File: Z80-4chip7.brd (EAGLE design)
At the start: 99.7 x 99.7 mm, 99 parts, among them IC1 Z84C00xx (-Z80-), IC2 CXK581000 (128k * 8), IC4 7400N, M1 WIRE-VIA8, U1 ATMEGA32A-PU

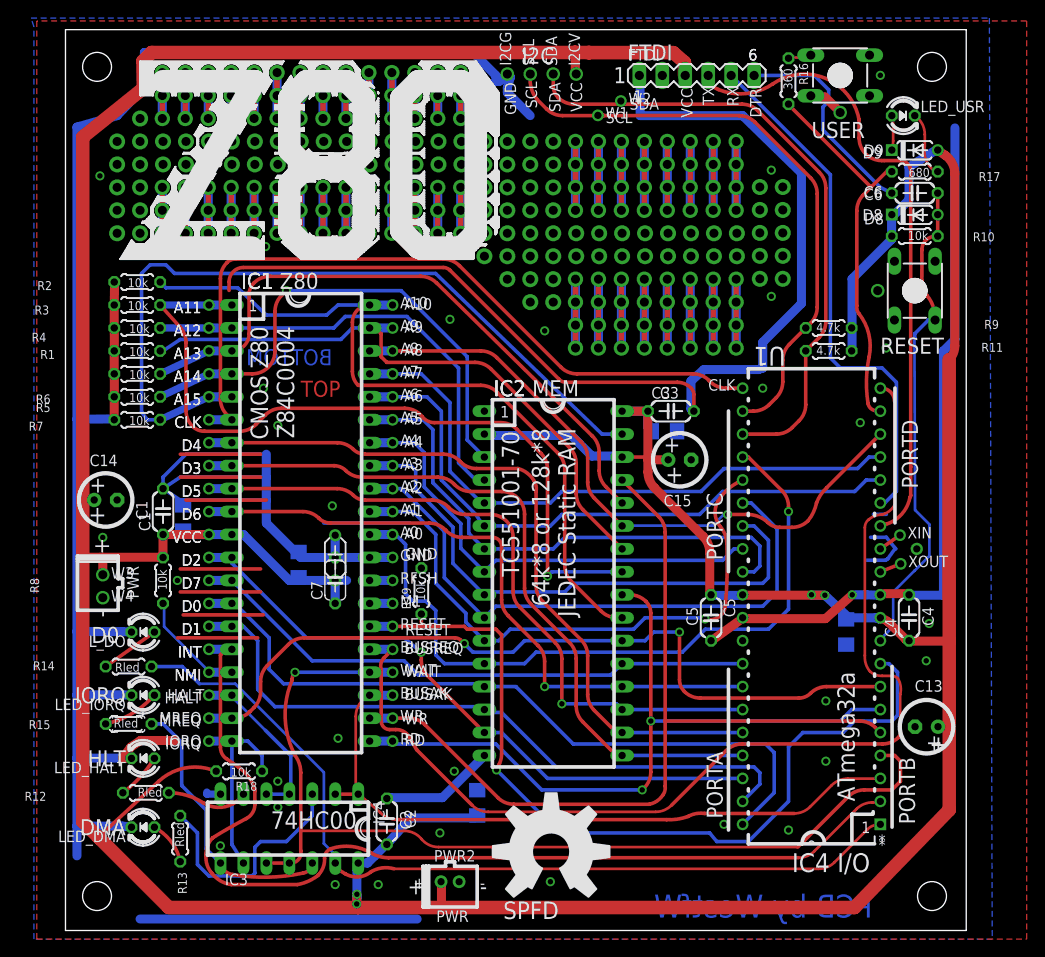
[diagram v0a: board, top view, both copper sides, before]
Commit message: Mod silkscreen: RTS->DTR, add "Version 2."  Generate Gerbers-V2.
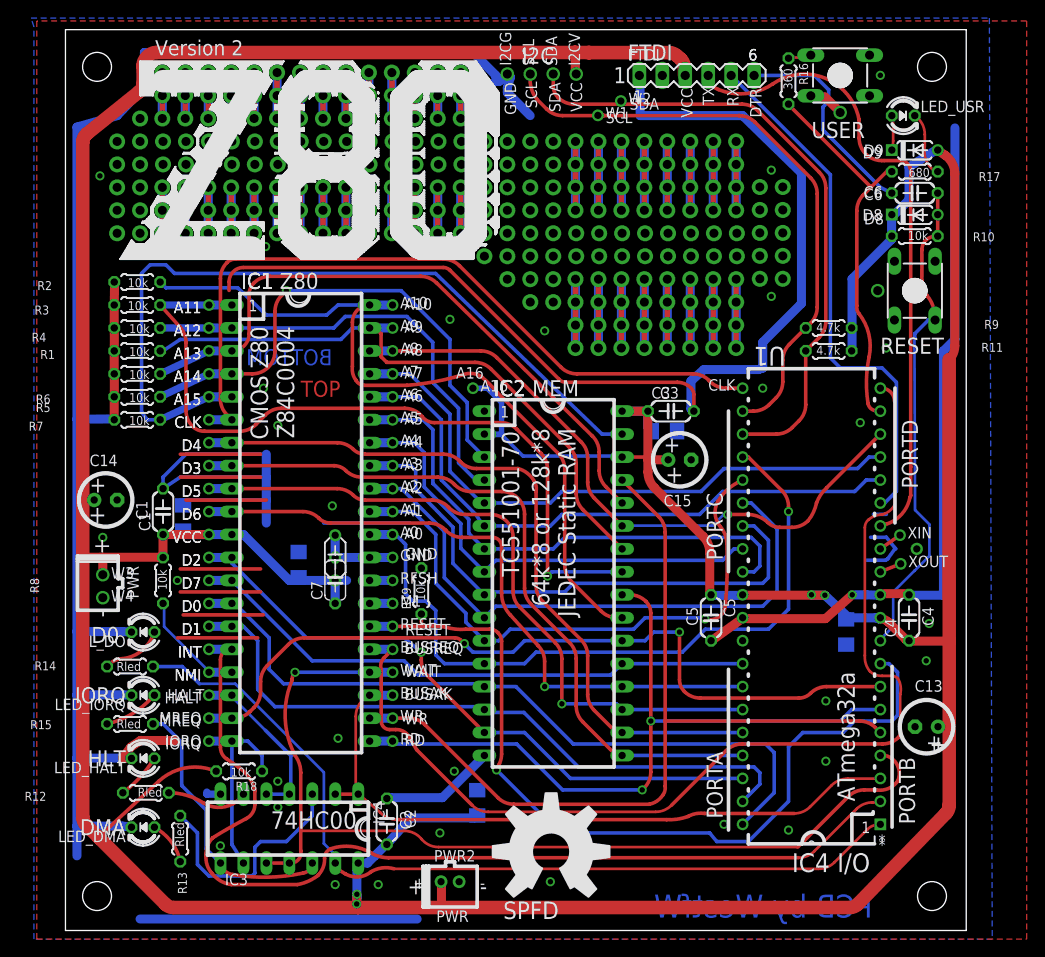
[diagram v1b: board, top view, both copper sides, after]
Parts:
- added A16: WIRE-VIA8, mylib4:VIA8
- moved R15 0.16 mm to (7.78, 22.9)
- moved R14 0.16 mm to (7.78, 29.2)
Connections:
- net VCC: now also A16.P$1
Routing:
- net GND: track 587.1 -> 575.6 mm
- net VCC: track 530.8 -> 539.2 mm
- net WAIT: track 109.4 -> 107.9 mm
- net A7: track 69.0 -> 68.3 mm
- net A6: track 69.1 -> 68.6 mm
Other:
- board text added: "20170228 by WestfW: "version 2" in silkscreen"
- board text added: "A16"
- board text added: "A16/Vcc"
- board text added: "Version 2"

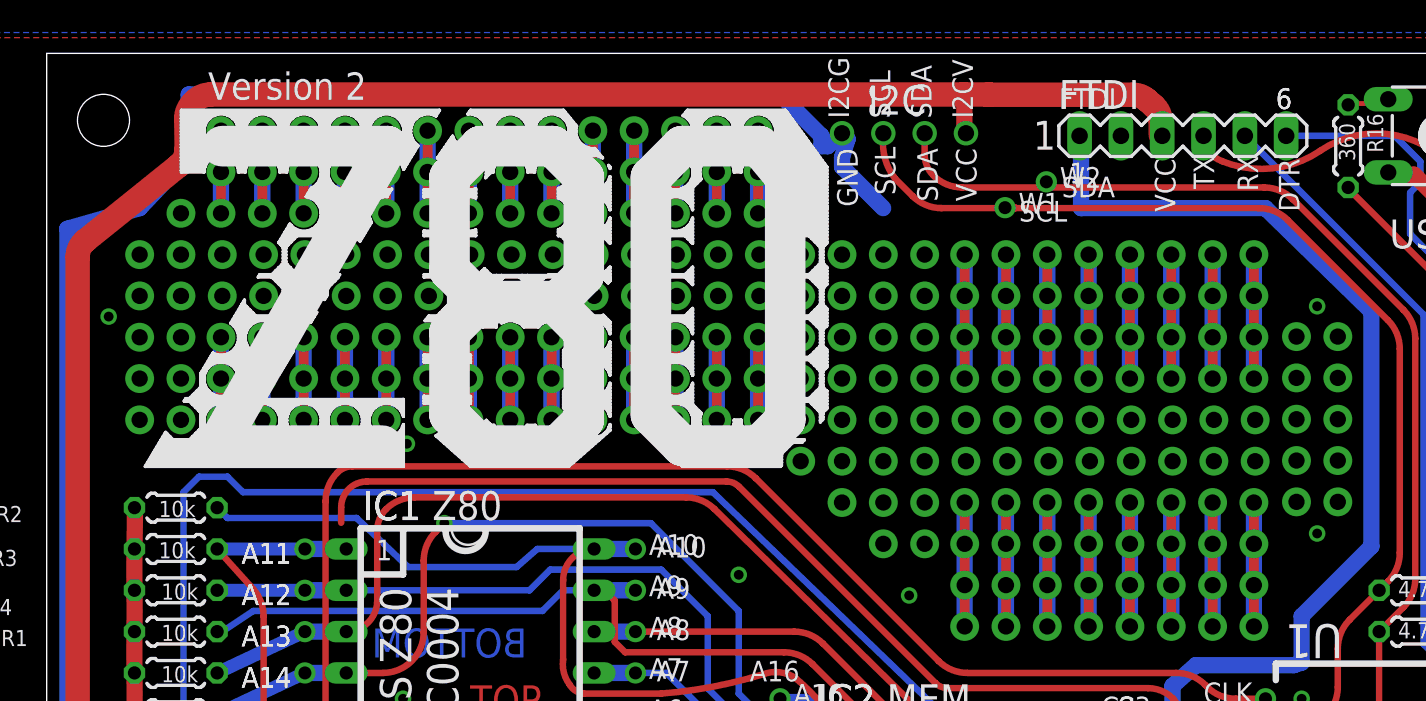
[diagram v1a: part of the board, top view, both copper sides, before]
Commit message: Modify Z80 brd to include power/gnd vias near prototype area. Add (untested) board designs for EEPROM floppy-emulation  module.
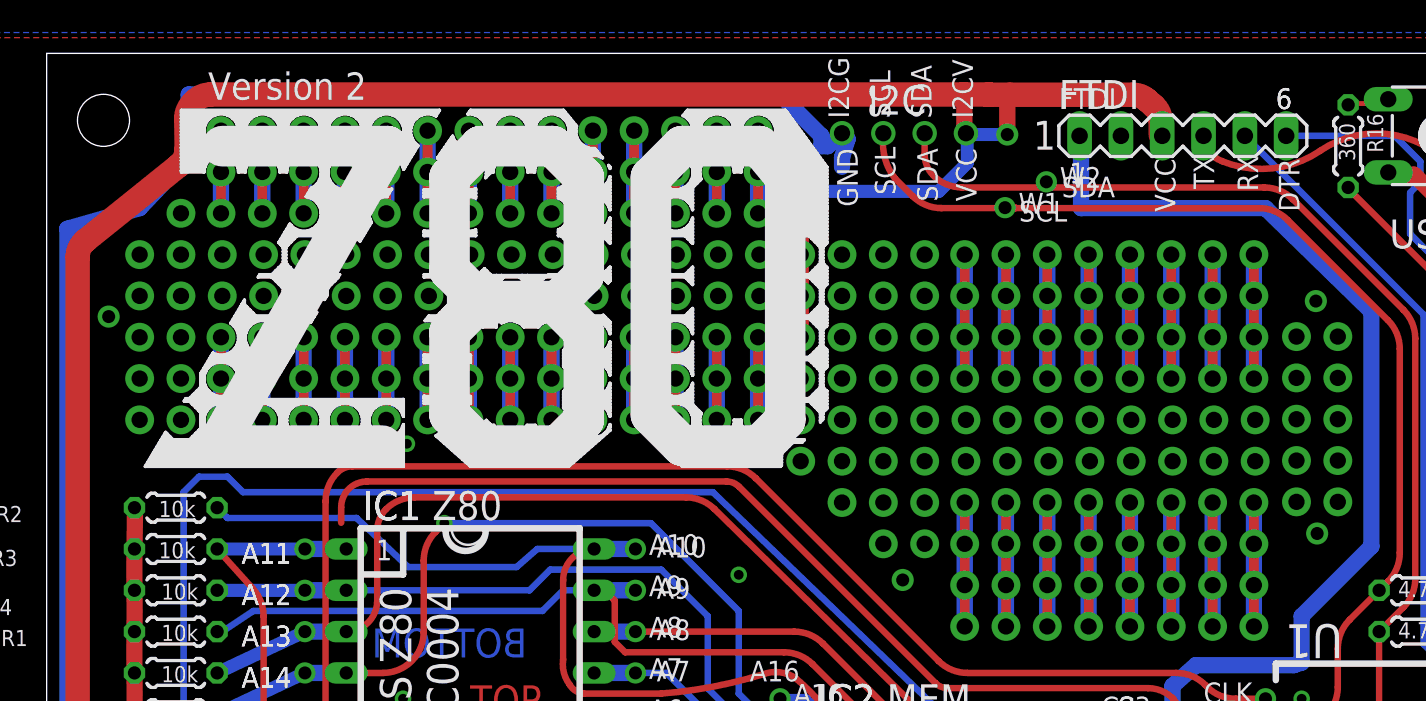
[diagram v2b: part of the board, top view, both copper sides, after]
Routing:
- net VCC: track 539.2 -> 573.0 mm, vias 5 -> 10
- net GND: track 575.6 -> 572.0 mm, vias 33 -> 36
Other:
- board text added: "20170512 by WestfW: Put some power and Gnd vias near the prototype area!"
- board text added: "R16 and R17 have the values swapped"
